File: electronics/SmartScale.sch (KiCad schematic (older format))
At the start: 68 parts, among them IC1 HX711, J2 Conn_01x06, J3 Conn_01x06, J4 Conn_01x04, P1 USB_C_Plug_USB2.0, Q1 BC847, Q2 BC847, Q3 IRLML0030, Q4 IRLML0030, Q5 MMBT3906, SW1 SW_Push_JTP-1130, SW2 SW_Push_JTP-1130, T9 TestPoint, U1 ESP32-WROOM-32, U2 TP4056, U3 DW01-P, U4 MIC37100

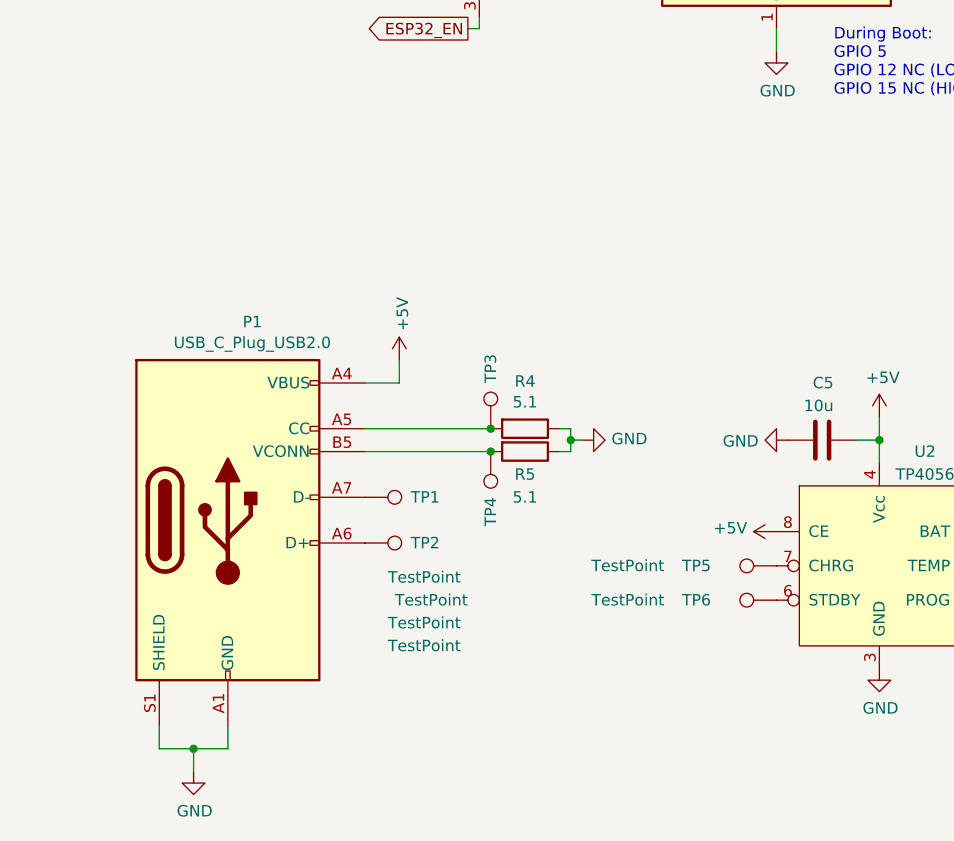
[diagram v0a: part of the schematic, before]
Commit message: Pushed casing and updated PCB
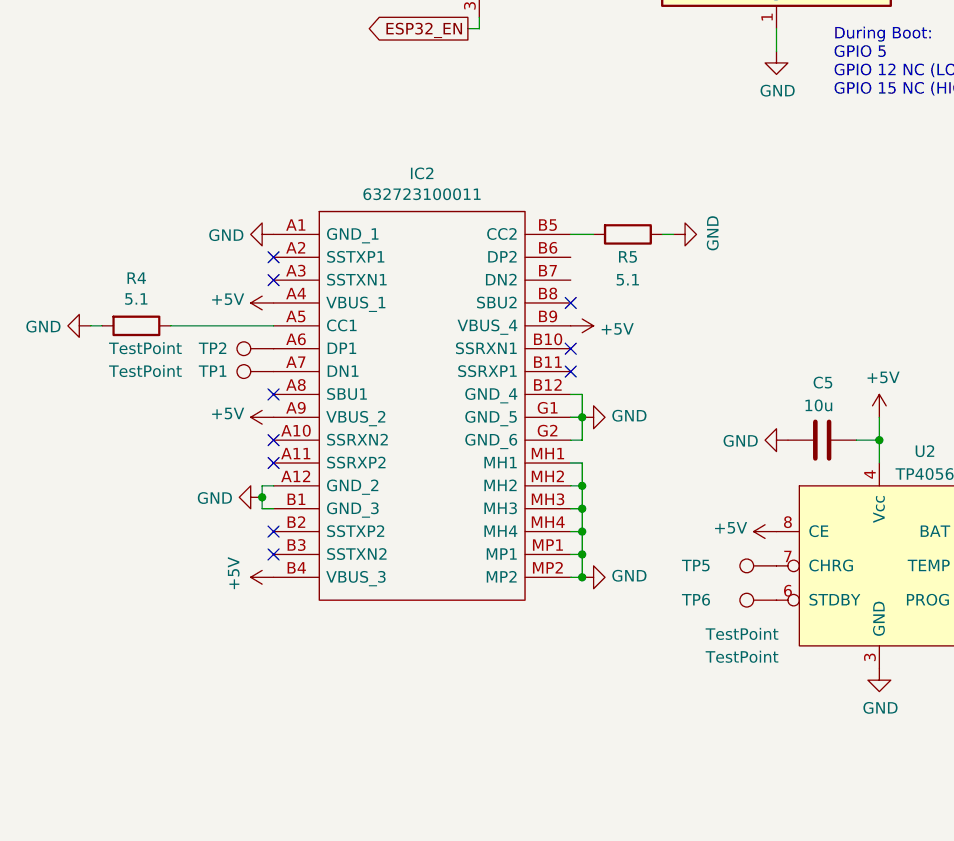
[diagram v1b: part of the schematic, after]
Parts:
- removed P1: USB_C_Plug_USB2.0, Connector_USB:USB_C_Receptacle_GCT_USB4085, symbol SmartScale-rescue:USB_C_Plug_USB2.0-Connector
- removed TP3, TP4: TestPoint, TestPoint:TestPoint_Pad_D1.0mm, symbol SmartScale-rescue:TestPoint-Connector
- added IC2: 632723100011, Wuerth:632723100011, symbol SmartScale-rescue:632723100011-Mouser
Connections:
- net +5V: now also IC2.A4 (VBUS_1), IC2.A9 (VBUS_2), IC2.B4 (VBUS_3), IC2.B9 (VBUS_4)
- net GND: now also R4.2, IC2.A1 (GND_1), IC2.A12 (GND_2), IC2.B1 (GND_3), IC2.B12 (GND_4), IC2.G1 (GND_5), IC2.G2 (GND_6), IC2.MH1, IC2.MH2, IC2.MH3, IC2.MH4, IC2.MP1, IC2.MP2; no longer R4.1
- net at TP2.1: now also IC2.A6 (DP1)
- net at TP1.1: now also IC2.A7 (DN1)
- net at R5.2: now also IC2.B5 (CC2)
- new net: IC2.A5 (CC1), R4.1
- no-connect marks 19 -> 29
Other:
- moved on the sheet: R4, R5, TP1, TP2

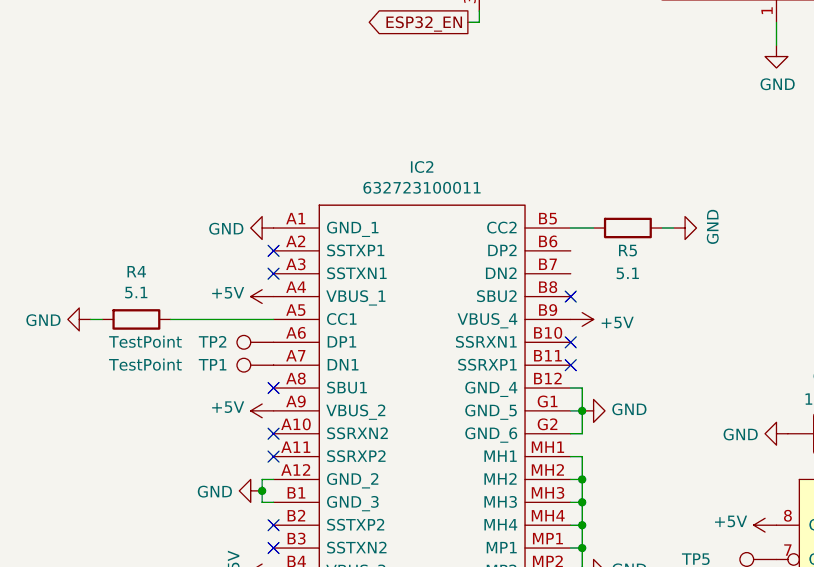
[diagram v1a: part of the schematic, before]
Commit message: PCB Rev 5
- Added 42Nibbles QR Code
- Moved 5V connection
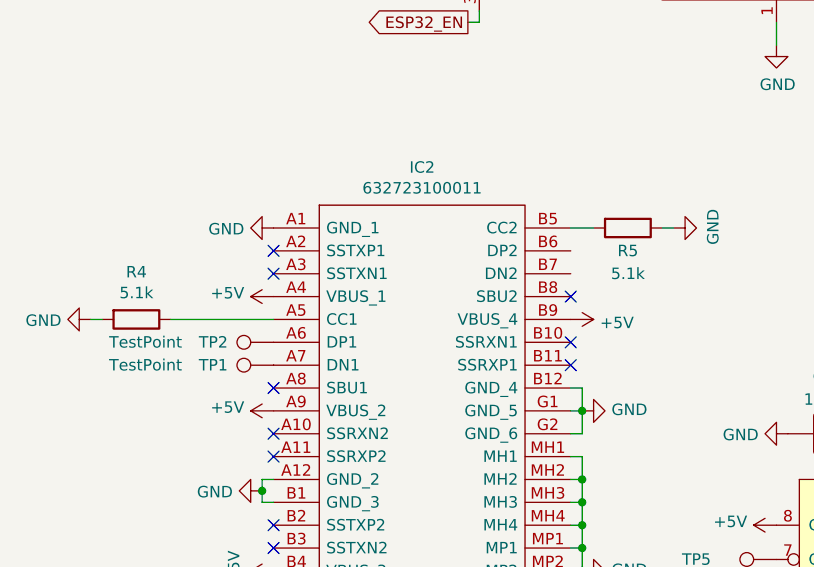
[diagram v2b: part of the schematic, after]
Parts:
- R4, R5: value 5.1 -> 5.1k
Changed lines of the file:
@@
 P 950 5500
 F 0 "R4" V 743 5500 50  0000 C CNN
-F 1 "5.1" V 834 5500 50  0000 C CNN
+F 1 "5.1k" V 834 5500 50  0000 C CNN
 F 2 "Resistor_SMD:R_0805_2012Metric_Pad1.20x1.40mm_HandSolder" V 880 5500 50  0001 C CNN
 F 3 "~" H 950 5500 50  0001 C CNN
@@
 P 3100 5100
 F 0 "R5" V 3200 5100 50  0000 C CNN
-F 1 "5.1" V 3300 5100 50  0000 C CNN
+F 1 "5.1k" V 3300 5100 50  0000 C CNN
 F 2 "Resistor_SMD:R_0805_2012Metric_Pad1.20x1.40mm_HandSolder" V 3030 5100 50  0001 C CNN
 F 3 "~" H 3100 5100 50  0001 C CNN
